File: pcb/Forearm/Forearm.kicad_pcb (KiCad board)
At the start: 4 copper layers, 102 x 122.4 mm, 9 parts, among them J2 Conn_01x12_Ribbon_To_Top, J3 Conn_01x12_To_Bottom, J4 Conn_01x03_DFR0205, U1 ESP32-S3-DEVKITC-1-N8R2, U2 4754

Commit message: completed tentative part layout
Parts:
- BT1: moved to B.Cu
- moved J4 178.7 mm to (14.3, 177.4), turned to 90 degrees
- moved C1 176.5 mm to (27.2, 79.1), turned to -90 degrees
- moved C2 155.4 mm to (48.3, 79.1), turned to -90 degrees
- moved BT1 150.8 mm to (37.4, 64.9), turned to 90 degrees
- moved U2 107.2 mm to (37.4, 55.7), turned to -90 degrees
- moved VR1 100.2 mm to (38.4, 80.3), turned to 90 degrees
- moved U1 80.8 mm to (37.4, 145.1)
- moved J3 28.5 mm to (50.8, 21.4)
- moved J2 24.0 mm to (23.9, 21.4)
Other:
- board size 102 x 122.4 mm -> 50.8 x 167.6 mm

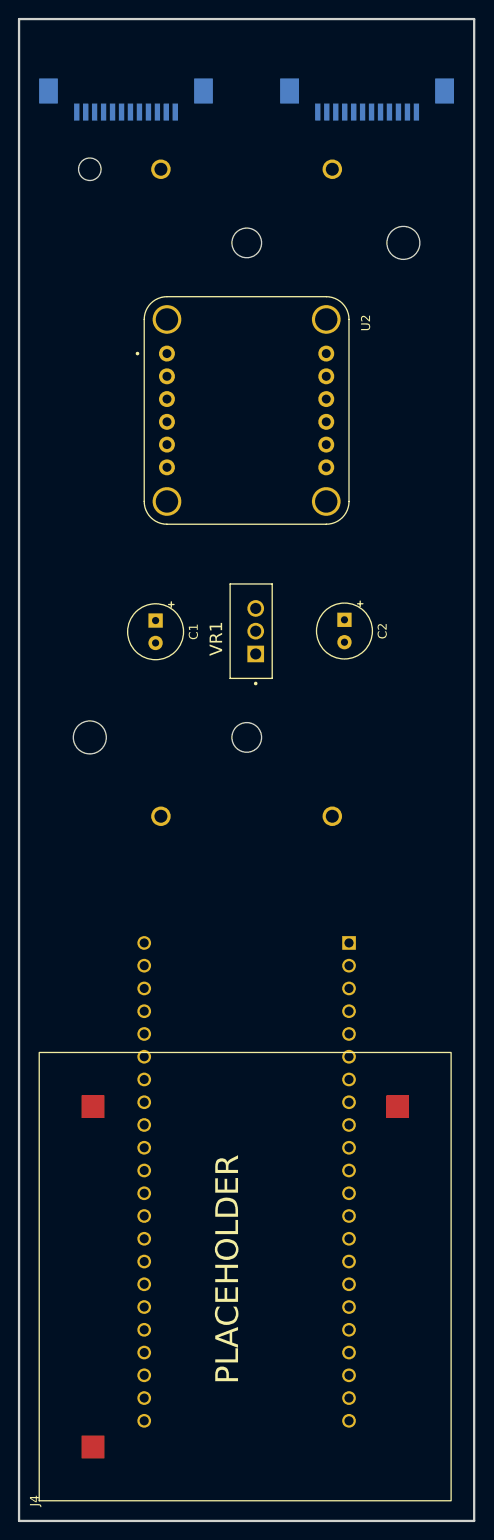
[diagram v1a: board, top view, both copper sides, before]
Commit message: revised hand and made pass at routing forearm pcb
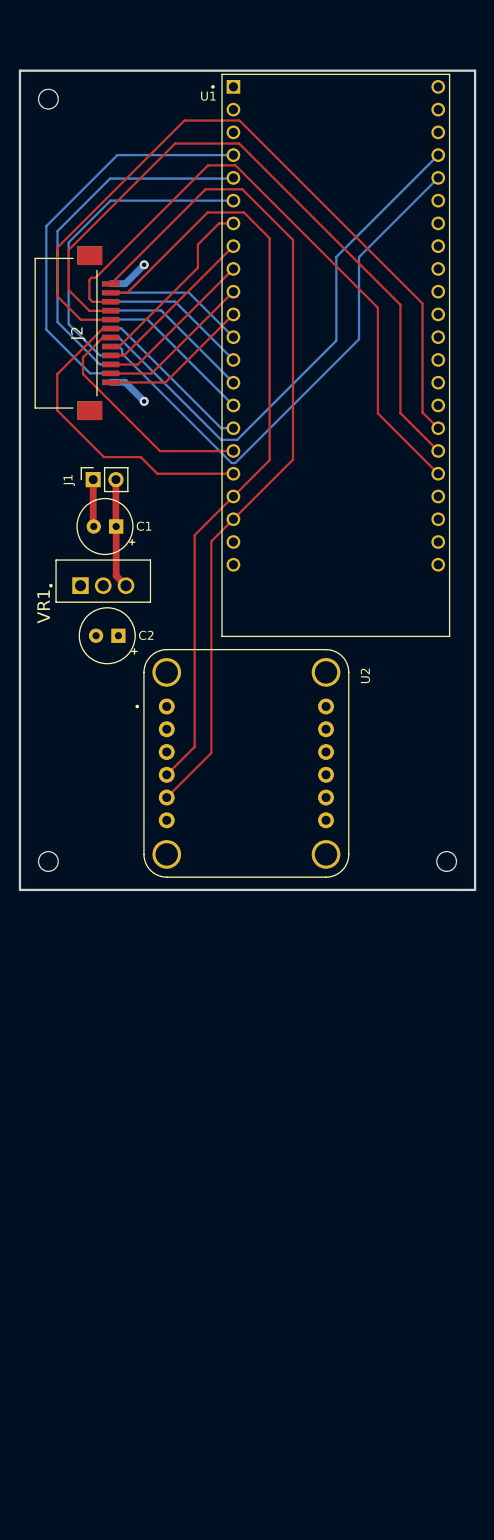
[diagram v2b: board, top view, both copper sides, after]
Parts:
- removed BT1: 1049, 1049:BAT_1049
- removed J4: Conn_01x03_DFR0205, DFR0205:DFR0205
- added J1: Conn_01x02, Connector_PinSocket_2.54mm:PinSocket_1x02_P2.54mm_Vertical, F.Cu at (20.3, 63.4)
- added REF**: MountingHole_2.2mm_M2, MountingHole:MountingHole_2.2mm_M2, F.Cu at (59.7, 106.0)
- added REF**: MountingHole_2.2mm_M2, MountingHole:MountingHole_2.2mm_M2, F.Cu at (15.3, 20.9)
- added REF**: MountingHole_2.2mm_M2, MountingHole:MountingHole_2.2mm_M2, F.Cu at (15.3, 106.0)
- J2, U1: moved to F.Cu
- moved U1 96.1 mm to (47.4, 49.5), turned to 0 degrees
- moved U2 39.4 mm to (37.4, 95.1)
- moved J3 39.1 mm to (21.3, 47.0), turned to 90 degrees
- moved J2 25.8 mm to (21.3, 47.1), turned to -90 degrees
- moved C2 25.3 mm to (23.1, 80.8), turned to 180 degrees
- moved VR1 17.8 mm to (21.4, 75.2), turned to 0 degrees
- moved C1 11.4 mm to (22.8, 68.6), turned to 180 degrees
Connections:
- C1 pad 2: GND -> 8V4_GND
- J2 pad 1: HAPTIC_S0 -> IMU_SDA
- J2 pad 10: FEEDBACK_D4 -> FEEDBACK_D2
- J2 pad 11: IMU_SCL -> FEEDBACK_D3
- J2 pad 12: IMU_SDA -> FEEDBACK_D4
- J2 pad 2: HAPTIC_S1 -> IMU_SCL
- J2 pad 4: HAPTIC_SCL -> HAPTIC_S1
- J2 pad 5: HAPTIC_SDA -> HAPTIC_S0
- J2 pad 6: FEEDBACK_D0 -> HAPTIC_SCL
- J2 pad 7: FEEDBACK_D1 -> HAPTIC_SDA
- J2 pad 8: FEEDBACK_D2 -> FEEDBACK_D0
- J2 pad 9: FEEDBACK_D3 -> FEEDBACK_D1
- J3 pad 10: SPOOLPOT_ADC3 -> HALL_S0
- J3 pad 11: SPOOLPOT_ADC4 -> HALL_ADC
- J3 pad 2: HALL_ADC -> SPOOLPOT_ADC4
- J3 pad 3: HALL_S0 -> SPOOLPOT_ADC3
- J3 pad 4: HALL_S1 -> SPOOLPOT_ADC2
- J3 pad 5: HALL_S2 -> SPOOLPOT_ADC1
- J3 pad 6: HALL_S3 -> SPOOLPOT_ADC0
- J3 pad 7: SPOOLPOT_ADC0 -> HALL_S3
- J3 pad 8: SPOOLPOT_ADC1 -> HALL_S2
- J3 pad 9: SPOOLPOT_ADC2 -> HALL_S1
- U1 pad J1_17: IMU_SDA -> HAPTIC_SDA
- U1 pad J1_18: IMU_SCL -> HAPTIC_SCL
- U1 pad J1_19: HAPTIC_SDA -> IMU_SCL
- U1 pad J1_20: HAPTIC_SCL -> IMU_SDA
- U1 pad J1_4: SPOOLPOT_ADC2 -> SPOOLPOT_ADC4
- U1 pad J1_6: SPOOLPOT_ADC4 -> SPOOLPOT_ADC2
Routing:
- net IMU_SDA: track 0.00 -> 95.1 mm
- net IMU_SCL: track 0.00 -> 87.3 mm
- net HAPTIC_S0: track 0.00 -> 82.2 mm
- net HAPTIC_S1: track 0.00 -> 77.6 mm
- net HAPTIC_S2: track 0.00 -> 70.0 mm
- net SPOOLPOT_ADC1: track 0.00 -> 60.8 mm
- net SPOOLPOT_ADC0: track 0.00 -> 59.9 mm
- net SPOOLPOT_ADC4: track 0.00 -> 44.9 mm
- net SPOOLPOT_ADC3: track 0.00 -> 40.1 mm
- net SPOOLPOT_ADC2: track 0.00 -> 35.6 mm
- net HAPTIC_SCL: track 0.00 -> 34.7 mm
- net HAPTIC_SDA: track 0.00 -> 26.4 mm
- net FEEDBACK_D0: track 0.00 -> 20.9 mm
- net FEEDBACK_D1: track 0.00 -> 18.7 mm
- net HALL_S3: track 0.00 -> 18.3 mm
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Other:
- board size 50.8 x 167.6 mm -> 50.8 x 91.4 mm

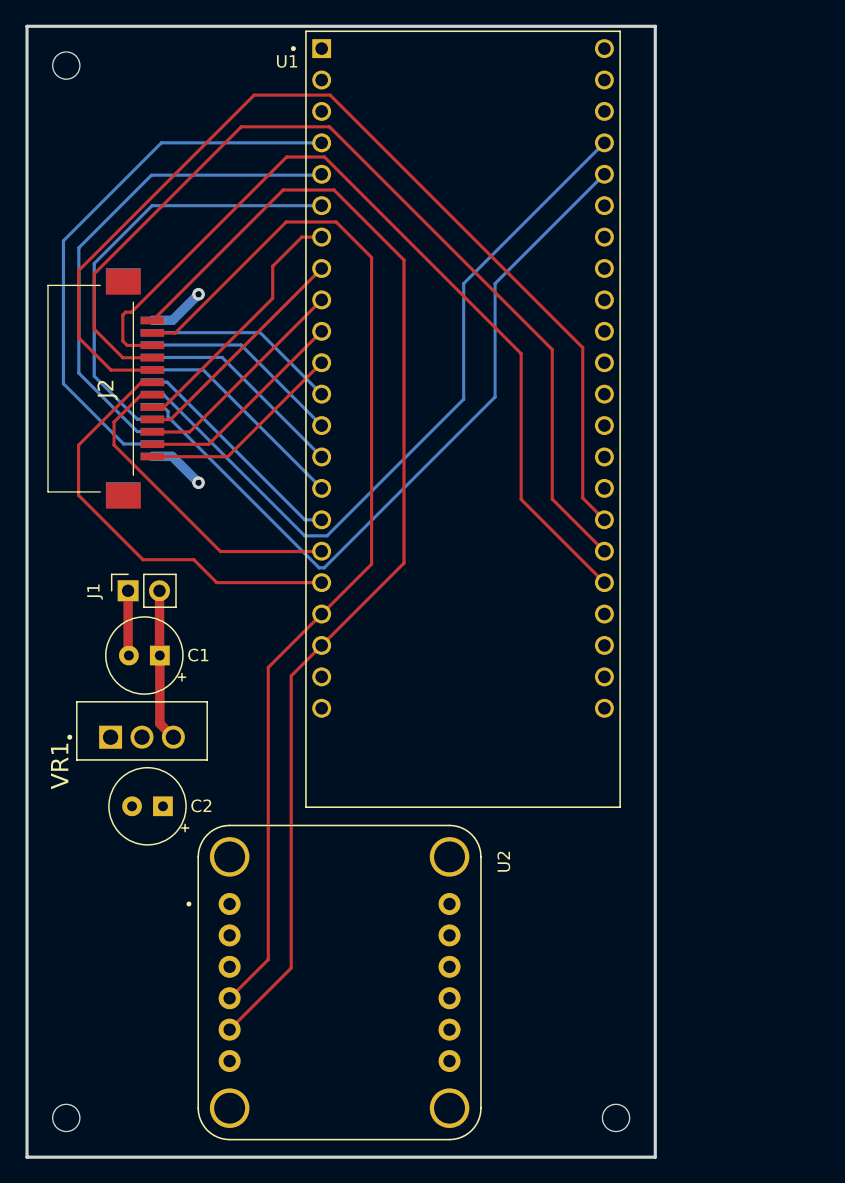
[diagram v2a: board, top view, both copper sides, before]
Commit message: re-did layout of forearm board
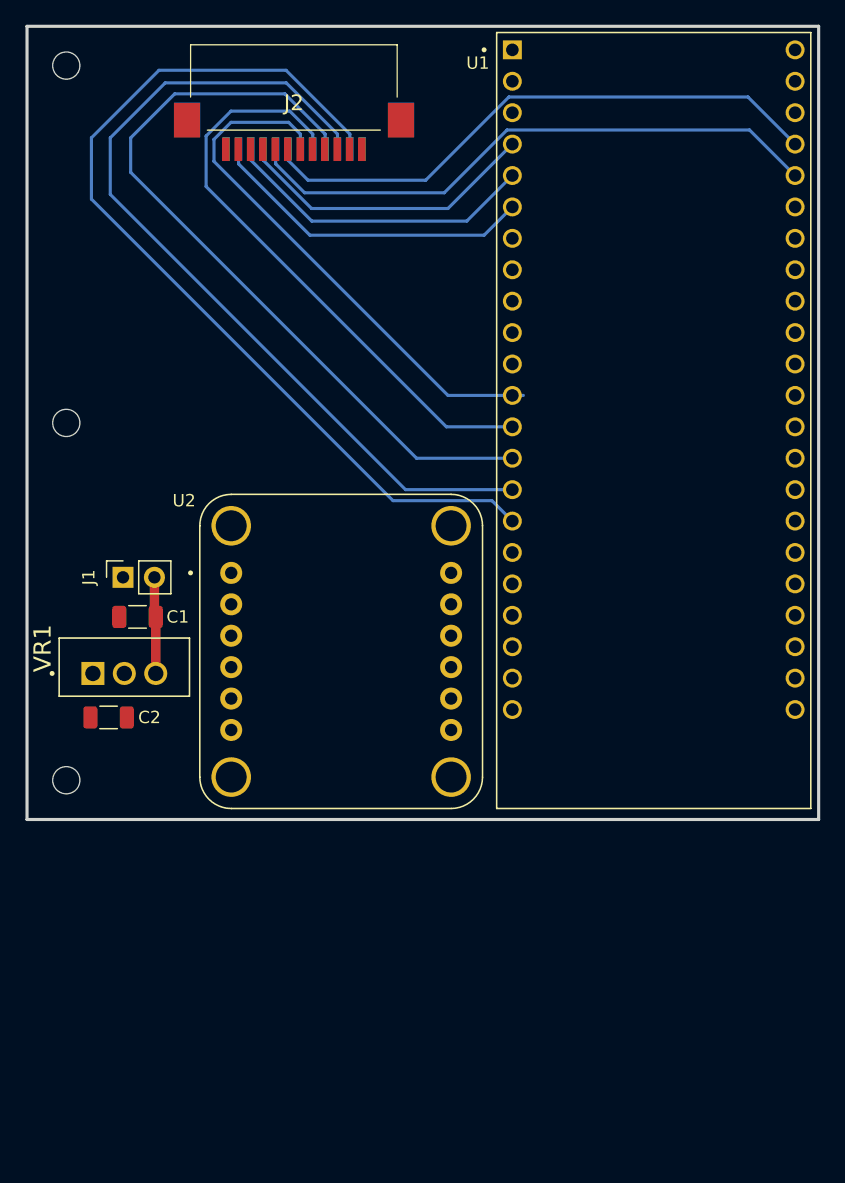
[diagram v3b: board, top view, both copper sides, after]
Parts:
- C1, C2: footprint Capacitor_THT:CP_Radial_Tantal_D6.0mm_P2.50mm -> Capacitor_SMD:C_1206_3216Metric
- moved REF** 71.7 mm to (15.3, 49.8)
- moved REF** 27.3 mm to (15.3, 78.7)
- moved U2 26.8 mm to (37.5, 68.3)
- moved J3 23.8 mm to (33.7, 26.7), turned to 0 degrees
- moved J2 23.8 mm to (33.7, 26.8), turned to 180 degrees
- moved U1 15.4 mm to (62.8, 49.6)
- moved C2 8.42 mm to (18.7, 73.6)
- moved VR1 5.35 mm to (20.0, 70.1)
- moved C1 3.61 mm to (21.0, 65.5)
- moved J1 1.17 mm to (19.9, 62.3)
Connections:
- C1 pad 2: 8V4_GND -> GND
- J1 pad 1: 8V4_GND -> GND
- U1 pad J1_12: HALL_ADC -> HALL_S3
- U1 pad J1_13: HALL_S0 -> HALL_S2
- U1 pad J1_15: HALL_S2 -> HALL_S0
- U1 pad J1_16: HALL_S3 -> HALL_ADC
- U1 pad J1_4: SPOOLPOT_ADC4 -> SPOOLPOT_ADC2
- U1 pad J1_6: SPOOLPOT_ADC2 -> SPOOLPOT_ADC4
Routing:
- net IMU_SDA: track 95.1 -> 0.00 mm
- net IMU_SCL: track 87.3 -> 0.00 mm
- net HAPTIC_S0: track 82.2 -> 0.00 mm
- net HAPTIC_S1: track 77.6 -> 0.00 mm
- net HAPTIC_S2: track 70.0 -> 0.00 mm
- net HALL_ADC: track 15.8 -> 76.3 mm
- net HALL_S0: track 16.4 -> 70.1 mm
- net HALL_S1: track 17.0 -> 63.0 mm
- net HAPTIC_SCL: track 34.7 -> 0.00 mm
- net HALL_S2: track 17.7 -> 48.3 mm
- net HAPTIC_SDA: track 26.4 -> 0.00 mm
- net HALL_S3: track 18.3 -> 43.8 mm
- net FEEDBACK_D0: track 20.9 -> 0.00 mm
- net FEEDBACK_D1: track 18.7 -> 0.00 mm
- net SPOOLPOT_ADC4: track 44.9 -> 26.7 mm
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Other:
- board size 50.8 x 91.4 mm -> 64 x 64.1 mm

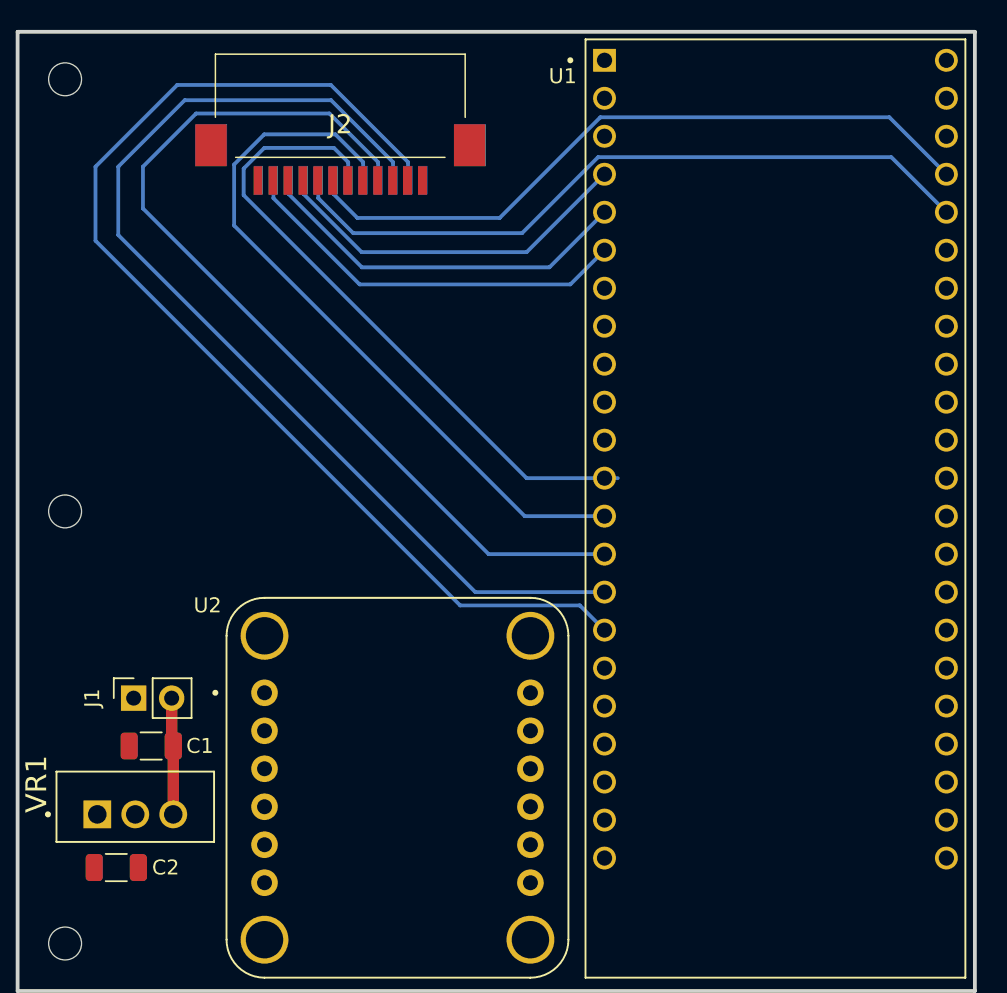
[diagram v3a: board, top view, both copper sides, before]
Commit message: re-routed forearm board w/o switches etc
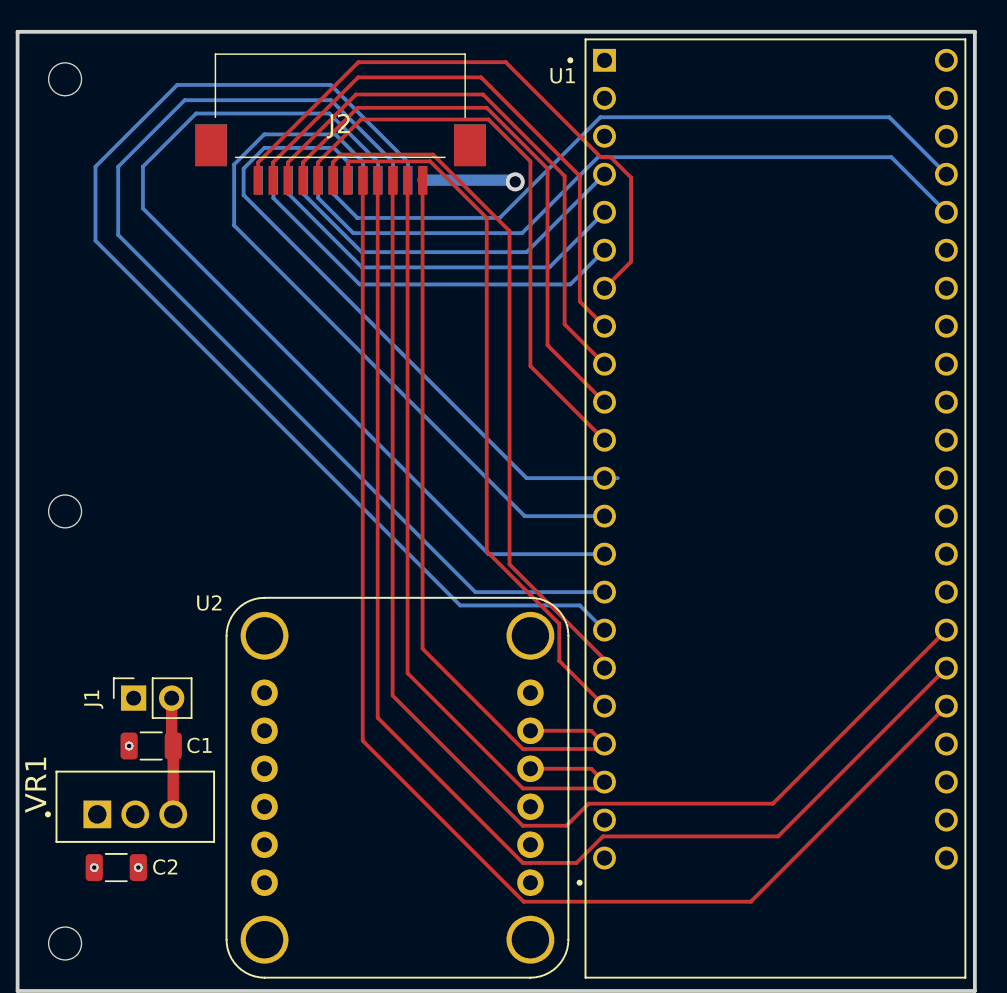
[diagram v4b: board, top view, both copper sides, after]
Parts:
- turned U2 to 90 degrees
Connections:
- J3 pad 1: GND -> FREE
- U1 pad J1_10: FEEDBACK_D3 -> FEEDBACK_D1
- U1 pad J1_11: FEEDBACK_D4 -> FEEDBACK_D0
- U1 pad J1_19: IMU_SCL -> IMU_SDA
- U1 pad J1_20: IMU_SDA -> IMU_SCL
- U1 pad J1_7: FEEDBACK_D0 -> FEEDBACK_D4
- U1 pad J1_8: FEEDBACK_D1 -> FEEDBACK_D3
- U1 pad J3_16: HAPTIC_S0 -> HAPTIC_S2
- U1 pad J3_18: HAPTIC_S2 -> HAPTIC_S0
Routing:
- net HAPTIC_S0: track 0.00 -> 86.4 mm
- net HAPTIC_S1: track 0.00 -> 83.4 mm
- net HAPTIC_S2: track 0.00 -> 80.5 mm
- net IMU_SCL: track 0.00 -> 54.8 mm
- net IMU_SDA: track 0.00 -> 51.7 mm
- net HAPTIC_SCL: track 0.00 -> 48.0 mm
- net HAPTIC_SDA: track 0.00 -> 47.2 mm
- net FEEDBACK_D4: track 0.00 -> 40.3 mm
- net FEEDBACK_D0: track 0.00 -> 38.5 mm
- net FEEDBACK_D1: track 0.00 -> 38.0 mm
- net FEEDBACK_D2: track 0.00 -> 37.5 mm
- net FEEDBACK_D3: track 0.00 -> 37.5 mm
- net 3V3: track 0.00 -> 6.22 mm, vias 0 -> 2
- net GND: vias 0 -> 2
